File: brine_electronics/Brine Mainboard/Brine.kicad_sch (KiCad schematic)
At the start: 14 parts, among them J1 Conn_01x02_Socket, J2 VL53L1X, U1 XIAO-ESP32-S3-SMD

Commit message: Created integrated distance sensor
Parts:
- removed BATT1: Conn_01x02_Pin, Connector_PinHeader_2.54mm:PinHeader_1x02_P2.54mm_Vertical, symbol Connector:Conn_01x02_Pin
- removed C1: 100uF, Capacitor_SMD:C_0805_2012Metric, symbol Device:C
- removed D1: WS2812B, LED_SMD:LED_WS2812B_PLCC4_5.0x5.0mm_P3.2mm, symbol LED:WS2812B
- removed H1, H2: MountingHole, MountingHole:MountingHole_3.2mm_M3, symbol Mechanical:MountingHole
- removed J1: Conn_01x02_Socket, Connector_JST:JST_PH_B2B-PH-K_1x02_P2.00mm_Vertical, symbol Connector:Conn_01x02_Socket
- removed J2: VL53L1X, Connector_PinHeader_2.54mm:PinHeader_1x06_P2.54mm_Vertical, symbol Connector:Conn_01x06_Pin
- removed R1: 220k, Resistor_SMD:R_0805_2012Metric, symbol Device:R
- removed R2: 100k, Resistor_SMD:R_0805_2012Metric, symbol Device:R
- removed R4: 330, Resistor_SMD:R_0805_2012Metric, symbol Device:R
- removed S1: TL3342F260QG, TL3342F160QG:SW_TL3342F160QG, symbol 5_2mm_Button:TL3342F260QG
- removed SCL1, SDA1: 2.2k, Resistor_SMD:R_0805_2012Metric, symbol Device:R
- removed U1: XIAO-ESP32-S3-SMD, Seeed Studio XIAO Series Library:XIAO-ESP32S3-DIP, symbol Seeed_Studio_XIAO_Series:XIAO-ESP32-S3-SMD
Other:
- added sheet Battery (brine_battery.kicad_sch)
- added sheet Battery Monitor (brine_battery_monitor.kicad_sch)
- added sheet Button (brine_button.kicad_sch)
- added sheet Distance Sensor (brine_distance_sensor.kicad_sch)
- added sheet RGB LED (brine_rgb_led.kicad_sch)
- added sheet XIAO ESP32-S3 (xiao_esp32-s3.kicad_sch)
- note removed: "Battery"
- note removed: "Battery Voltage Divider"
- note removed: "Button"
- note removed: "Distance Sensor"
- note removed: "I2C Pullups"
- note removed: "RGB LED"
- note removed: "XIAO ESP32-S3"

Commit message: Implemented power latch circuit ⚡
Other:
- sheet XIAO ESP32-S3 renamed XIAO ESP32-C3
- added sheet Power Latch (power_latch.kicad_sch)
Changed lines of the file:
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@@
 	(wire
 		(pts
-			(xy 342.9 271.78) (xy 368.3 271.78)
-		)
-		(stroke
-			(width 0)
-			(type default)
-		)
-	)
-	(wire
-		(pts
-			(xy 342.9 276.86) (xy 368.3 276.86)
-		)
-		(stroke
-			(width 0)
-			(type default)
-		)
-	)
-	(wire
-		(pts
-			(xy 190.5 203.2) (xy 215.9 203.2)
-		)
-		(stroke
-			(width 0)
-			(type default)
-		)
-	)
-	(wire
-		(pts
-			(xy 279.4 152.4) (xy 279.4 177.8)
-		)
-		(stroke
-			(width 0)
-			(type default)
-		)
-	)
-	(wire
-		(pts
-			(xy 342.9 203.2) (xy 368.3 203.2)
-		)
-		(stroke
-			(width 0)
-			(type default)
-		)
-	)
-	(wire
-		(pts
-			(xy 190.5 279.4) (xy 215.9 279.4)
-		)
-		(stroke
-			(width 0)
-			(type default)
-		)
-	)
-	(wire
-		(pts
-			(xy 342.9 281.94) (xy 368.3 281.94)
-		)
-		(stroke
-			(width 0)
-			(type default)
-		)
-	)
-	(wire
-		(pts
-			(xy 342.9 287.02) (xy 368.3 287.02)
-		)
-		(stroke
-			(width 0)
-			(type default)
-		)
-	)
-	(sheet
-		(at 368.3 254)
+			(xy 342.9 309.88) (xy 368.3 309.88)
+		)
+		(stroke
+			(width 0)
+			(type default)
+		)
+	)
+	(wire
+		(pts
+			(xy 342.9 314.96) (xy 368.3 314.96)
+		)
+		(stroke
+			(width 0)
+			(type default)
+		)
+	)
+	(wire
+		(pts
+			(xy 190.5 241.3) (xy 215.9 241.3)
+		)
+		(stroke
+			(width 0)
+			(type default)
+		)
+	)
+	(wire
+		(pts
+			(xy 342.9 241.3) (xy 368.3 241.3)
+		)
+		(stroke
+			(width 0)
+			(type default)
+		)
+	)
+	(wire
+		(pts
+			(xy 190.5 317.5) (xy 215.9 317.5)
+		)
+		(stroke
+			(width 0)
+			(type default)
+		)
+	)
+	(wire
+		(pts
+			(xy 342.9 320.04) (xy 368.3 320.04)
+		)
+		(stroke
+			(width 0)
+			(type default)
+		)
+	)
+	(wire
+		(pts
+			(xy 342.9 325.12) (xy 368.3 325.12)
+		)
+		(stroke
+			(width 0)
+			(type default)
+		)
+	)
+	(sheet
+		(at 368.3 292.1)
 		(size 127 50.8)
 		(exclude_from_sim no)
@@
 		)
 		(property "Sheetname" "Distance Sensor"
-			(at 368.3 253.2884 0)
+			(at 368.3 291.3884 0)
 			(effects
 				(font
@@
 		)
 		(property "Sheetfile" "brine_distance_sensor.kicad_sch"
-			(at 368.3 305.3846 0)
+			(at 368.3 343.4846 0)
 			(effects
 				(font
@@
 		)
 		(pin "GPIO1" input
-			(at 368.3 271.78 180)
+			(at 368.3 309.88 180)
 			(effects
 				(font
@@
 		)
 		(pin "SCL" input
-			(at 368.3 276.86 180)
+			(at 368.3 314.96 180)
 			(effects
 				(font
@@
 		)
 		(pin "SDA" input
-			(at 368.3 281.94 180)
+			(at 368.3 320.04 180)
 			(effects
 				(font
@@
 		)
 		(pin "XSHUT" input
-			(at 368.3 287.02 180)
+			(at 368.3 325.12 180)
 			(effects
 				(font
@@
 	)
 	(sheet
-		(at 63.5 177.8)
+		(at 215.9 114.3)
+		(size 127 63.5)
+		(exclude_from_sim no)
+		(in_bom yes)
+		(on_board yes)
+		(dnp no)
+		(fields_autoplaced yes)
+		(stroke
+			(width 0.1524)
+			(type solid)
+		)
+		(fill
+			(color 0 0 0 0.0000)
+		)
+		(property "Sheetname" "Power Latch"
+			(at 215.9 113.5884 0)
+			(effects
+				(font
+					(size 1.27 1.27)
+				)
+				(justify left bottom)
+			)
+		)
+		(property "Sheetfile" "power_latch.kicad_sch"
+			(at 215.9 178.3846 0)
+			(effects
+				(font
+					(size 1.27 1.27)
+				)
+				(justify left top)
+			)
+		)
+		(instances
+			(project "Brine"
+				(path "/da3a4ef2-0e38-46f1-a1fc-55d8e0a83a54"
+					(page "8")
+				)
+			)
+		)
+	)
+	(sheet
+		(at 63.5 215.9)
 		(size 127 50.8)
 		(exclude_from_sim no)
@@
 		)
 		(property "Sheetname" "Button"
-			(at 63.5 177.0884 0)
+			(at 63.5 215.1884 0)
 			(effects
 				(font
@@
 		)
 		(property "Sheetfile" "brine_button.kicad_sch"
-			(at 63.5 229.1846 0)
+			(at 63.5 267.2846 0)
 			(effects
 				(font
@@
 		)
 		(pin "BUTTON" output
-			(at 190.5 203.2 0)
+			(at 190.5 241.3 0)
 			(effects
 				(font
@@
 	)
 	(sheet
-		(at 215.9 177.8)
+		(at 215.9 215.9)
 		(size 127 128.27)
 		(exclude_from_sim no)
@@
 			(color 0 0 0 0.0000)
 		)
-		(property "Sheetname" "XIAO ESP32-S3"
-			(at 215.9 177.0884 0)
+		(property "Sheetname" "XIAO ESP32-C3"
+			(at 215.9 215.1884 0)
 			(effects
 				(font
@@
 		)
 		(property "Sheetfile" "xiao_esp32-s3.kicad_sch"
-			(at 215.9 306.6546 0)
+			(at 215.9 344.7546 0)
 			(effects
 				(font
@@
 		)
 		(pin "LIFE" input
-			(at 215.9 279.4 180)
+			(at 215.9 317.5 180)
 			(effects
 				(font
@@
 		)
 		(pin "BATT" input
-			(at 279.4 177.8 90)
+			(at 279.4 215.9 90)
 			(effects
 				(font
@@
 		)
 		(pin "BUTTON" input
-			(at 215.9 203.2 180)
+			(at 215.9 241.3 180)
 			(effects
 				(font
@@
 		)
 		(pin "GPIO1" output
-			(at 342.9 271.78 0)
+			(at 342.9 309.88 0)
 			(effects
 				(font
@@
 		)
 		(pin "LED" output
-			(at 342.9 203.2 0)
+			(at 342.9 241.3 0)
 			(effects
 				(font
@@
 		)
 		(pin "SCL" output
-			(at 342.9 276.86 0)
+			(at 342.9 314.96 0)
 			(effects
 				(font
@@
 		)
 		(pin "SDA" output
-			(at 342.9 281.94 0)
+			(at 342.9 320.04 0)
 			(effects
 				(font
@@
 		)
 		(pin "XSHUT" output
-			(at 342.9 287.02 0)
+			(at 342.9 325.12 0)
 			(effects
 				(font
@@
 	)
 	(sheet
-		(at 368.3 177.8)
+		(at 368.3 215.9)
 		(size 127 50.8)
 		(exclude_from_sim no)
@@
 		)
 		(property "Sheetname" "RGB LED"
-			(at 368.3 177.0884 0)
+			(at 368.3 215.1884 0)
 			(effects
 				(font
@@
 		)
 		(property "Sheetfile" "brine_rgb_led.kicad_sch"
-			(at 368.3 229.1846 0)
+			(at 368.3 267.2846 0)
 			(effects
 				(font
@@
 		)
 		(pin "LED" input
-			(at 368.3 203.2 180)
+			(at 368.3 241.3 180)
 			(effects
 				(font
@@
 	)
 	(sheet
-		(at 215.9 101.6)
+		(at 215.9 39.37)
 		(size 127 50.8)
 		(exclude_from_sim no)
@@
 		)
 		(property "Sheetname" "Battery"
-			(at 215.9 100.8884 0)
+			(at 215.9 38.6584 0)
 			(effects
 				(font
@@
 		)
 		(property "Sheetfile" "brine_battery.kicad_sch"
-			(at 215.9 152.9846 0)
+			(at 215.9 90.7546 0)
 			(effects
 				(font
@@
 		)
 		(pin "BATT" output
-			(at 279.4 152.4 270)
+			(at 279.4 90.17 270)
 			(effects
 				(font
@@
 	)
 	(sheet
-		(at 63.5 254)
+		(at 63.5 292.1)
 		(size 127 50.8)
 		(exclude_from_sim no)
@@
 		)
 		(property "Sheetname" "Battery Monitor"
-			(at 63.5 253.2884 0)
+			(at 63.5 291.3884 0)
 			(effects
 				(font
@@
 		)
 		(property "Sheetfile" "brine_battery_monitor.kicad_sch"
-			(at 63.5 305.3846 0)
+			(at 63.5 343.4846 0)
 			(effects
 				(font
@@
 		)
 		(pin "LIFE" output
-			(at 190.5 279.4 0)
-			(effects
-				(font
+			(at 190.5 317.5 0)
+			(effects
+				(font

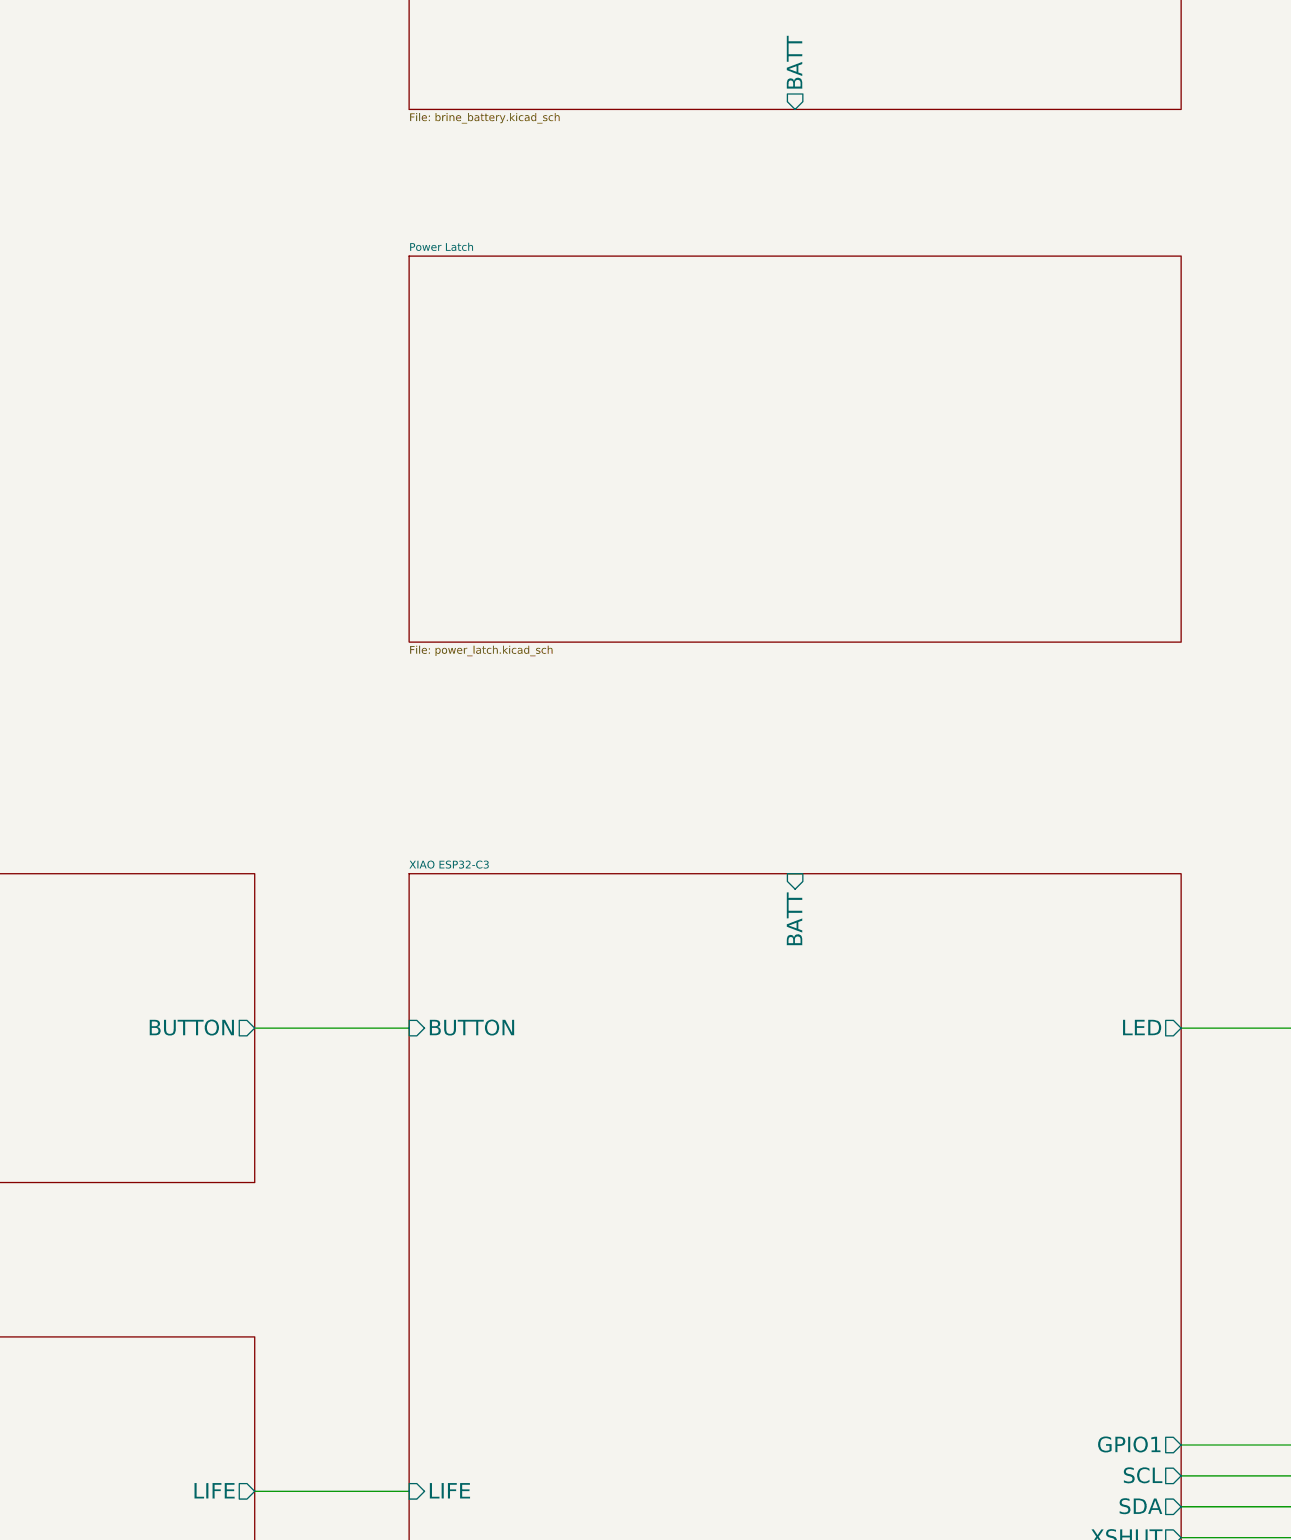
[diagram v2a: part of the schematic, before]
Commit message: Resolved schematic DRC issues ✅
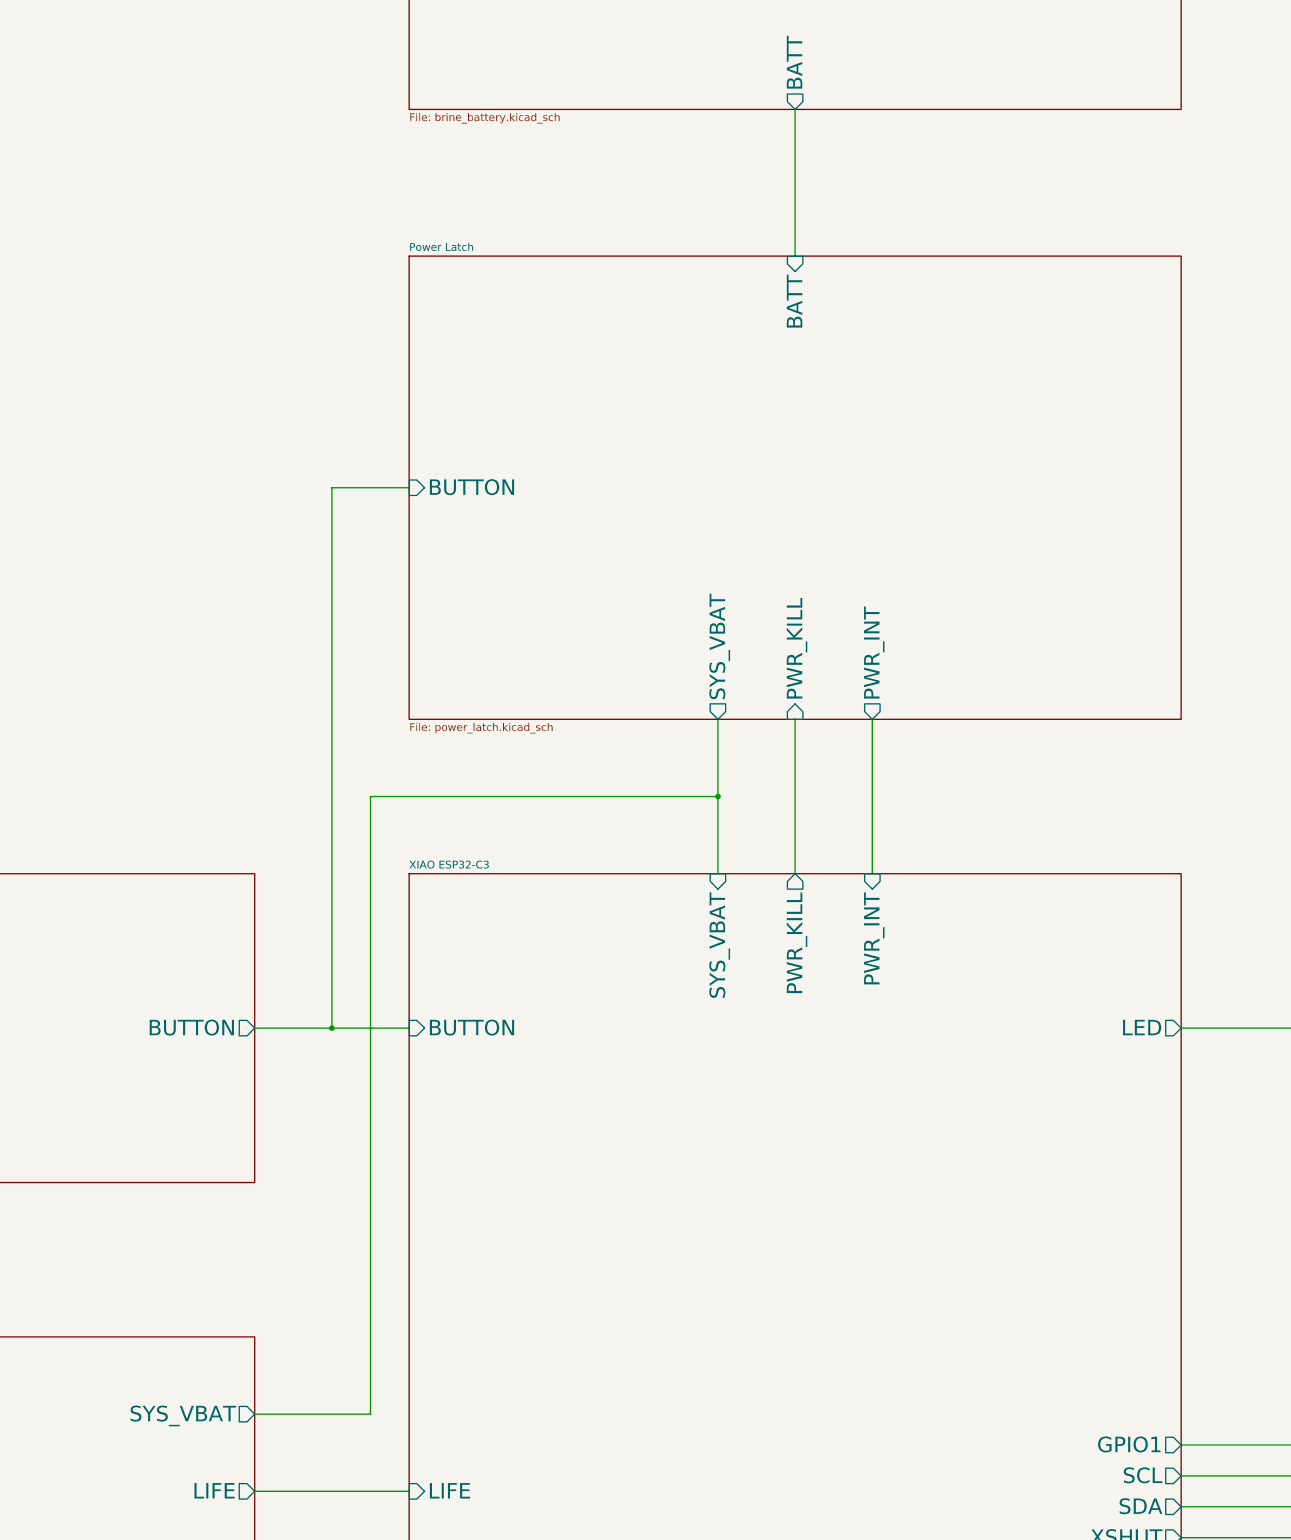
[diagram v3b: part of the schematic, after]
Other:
- sheet Battery Monitor ports: added SYS_VBAT; removed none
- sheet Power Latch ports: added BATT, BUTTON, PWR_INT, PWR_KILL, SYS_VBAT; removed none
- sheet XIAO ESP32-C3 ports: added PWR_INT, PWR_KILL, SYS_VBAT; removed BATT
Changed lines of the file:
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@@
 	(title_block
 		(title "Brine Monitor")
-		(date "2025-10-30")
-		(rev "Proto")
+		(date "2026-04-07")
+		(rev "1.0.0")
+	)
+	(junction
+		(at 203.2 241.3)
+		(diameter 0)
+		(color 0 0 0 0)
+	)
+	(junction
+		(at 266.7 203.2)
+		(diameter 0)
+		(color 0 0 0 0)
+	)
+	(wire
+		(pts
+			(xy 203.2 241.3) (xy 215.9 241.3)
+		)
+		(stroke
+			(width 0)
+			(type default)
+		)
+	)
+	(wire
+		(pts
+			(xy 279.4 190.5) (xy 279.4 215.9)
+		)
+		(stroke
+			(width 0)
+			(type default)
+		)
 	)
 	(wire
@@
 	(wire
 		(pts
+			(xy 209.55 304.8) (xy 209.55 203.2)
+		)
+		(stroke
+			(width 0)
+			(type default)
+		)
+	)
+	(wire
+		(pts
+			(xy 266.7 203.2) (xy 266.7 215.9)
+		)
+		(stroke
+			(width 0)
+			(type default)
+		)
+	)
+	(wire
+		(pts
 			(xy 342.9 314.96) (xy 368.3 314.96)
 		)
@@
 	(wire
 		(pts
-			(xy 190.5 241.3) (xy 215.9 241.3)
+			(xy 190.5 241.3) (xy 203.2 241.3)
+		)
+		(stroke
+			(width 0)
+			(type default)
+		)
+	)
+	(wire
+		(pts
+			(xy 190.5 304.8) (xy 209.55 304.8)
+		)
+		(stroke
+			(width 0)
+			(type default)
+		)
+	)
+	(wire
+		(pts
+			(xy 292.1 190.5) (xy 292.1 215.9)
+		)
+		(stroke
+			(width 0)
+			(type default)
+		)
+	)
+	(wire
+		(pts
+			(xy 279.4 90.17) (xy 279.4 114.3)
 		)
 		(stroke
@@
 	(wire
 		(pts
+			(xy 266.7 190.5) (xy 266.7 203.2)
+		)
+		(stroke
+			(width 0)
+			(type default)
+		)
+	)
+	(wire
+		(pts
 			(xy 342.9 325.12) (xy 368.3 325.12)
+		)
+		(stroke
+			(width 0)
+			(type default)
+		)
+	)
+	(wire
+		(pts
+			(xy 203.2 152.4) (xy 215.9 152.4)
+		)
+		(stroke
+			(width 0)
+			(type default)
+		)
+	)
+	(wire
+		(pts
+			(xy 203.2 241.3) (xy 203.2 152.4)
+		)
+		(stroke
+			(width 0)
+			(type default)
+		)
+	)
+	(wire
+		(pts
+			(xy 209.55 203.2) (xy 266.7 203.2)
 		)
 		(stroke
@@
 	(sheet
 		(at 215.9 114.3)
-		(size 127 63.5)
+		(size 127 76.2)
 		(exclude_from_sim no)
 		(in_bom yes)
@@
 		)
 		(property "Sheetfile" "power_latch.kicad_sch"
-			(at 215.9 178.3846 0)
+			(at 215.9 191.0846 0)
 			(effects
 				(font
@@
 				)
 				(justify left top)
+			)
+		)
+		(pin "BATT" input
+			(at 279.4 114.3 90)
+			(effects
+				(font
+					(size 2.54 2.54)
+				)
+				(justify right)
+			)
+		)
+		(pin "BUTTON" input
+			(at 215.9 152.4 180)
+			(effects
+				(font
+					(size 2.54 2.54)
+				)
+				(justify left)
+			)
+		)
+		(pin "PWR_INT" output
+			(at 292.1 190.5 270)
+			(effects
+				(font
+					(size 2.54 2.54)
+				)
+				(justify left)
+			)
+		)
+		(pin "PWR_KILL" input
+			(at 279.4 190.5 270)
+			(effects
+				(font
+					(size 2.54 2.54)
+				)
+				(justify left)
+			)
+		)
+		(pin "SYS_VBAT" output
+			(at 266.7 190.5 270)
+			(effects
+				(font
+					(size 2.54 2.54)
+				)
+				(justify left)
 			)
 		)
@@
 			)
 		)
-		(pin "BATT" input
-			(at 279.4 215.9 90)
-			(effects
-				(font
-					(size 2.54 2.54)
-				)
-				(justify right)
-			)
-		)
 		(pin "BUTTON" input
 			(at 215.9 241.3 180)
@@
 		(pin "XSHUT" output
 			(at 342.9 325.12 0)
+			(effects
+				(font
+					(size 2.54 2.54)
+				)
+				(justify right)
+			)
+		)
+		(pin "PWR_INT" input
+			(at 292.1 215.9 90)
+			(effects
+				(font
+					(size 2.54 2.54)
+				)
+				(justify right)
+			)
+		)
+		(pin "PWR_KILL" output
+			(at 279.4 215.9 90)
+			(effects
+				(font
+					(size 2.54 2.54)
+				)
+				(justify right)
+			)
+		)
+		(pin "SYS_VBAT" input
+			(at 266.7 215.9 90)
 			(effects
 				(font
@@
 			(effects
 				(font
+					(size 2.54 2.54)
+				)
+				(justify right)
+			)
+		)
+		(pin "SYS_VBAT" output
+			(at 190.5 304.8 0)
+			(effects
+				(font
